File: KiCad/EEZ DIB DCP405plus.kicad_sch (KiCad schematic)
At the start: 20 parts

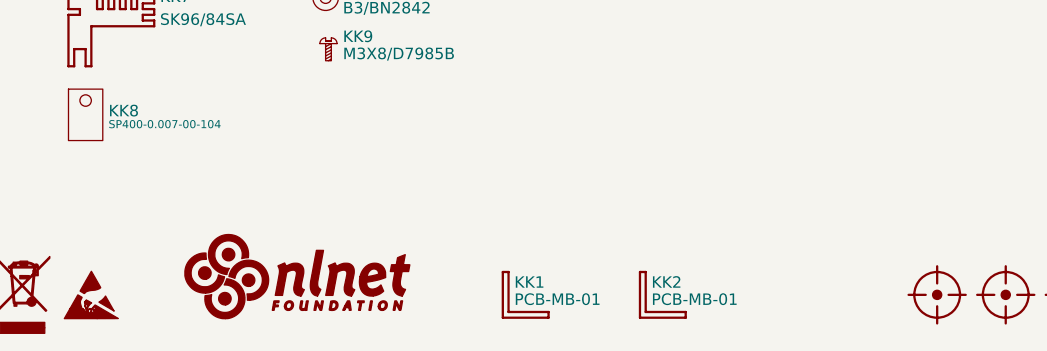
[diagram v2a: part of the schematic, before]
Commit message: OSHWA logo added, KiCad 10 migration
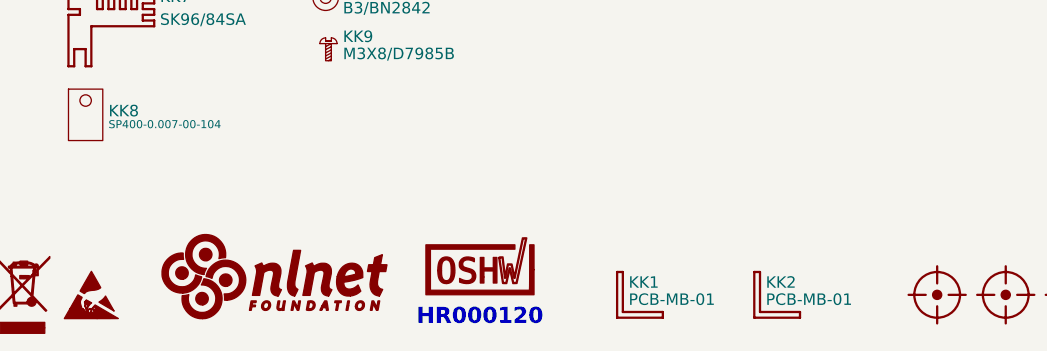
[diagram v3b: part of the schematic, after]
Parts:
- added LOGO7: OSHWA logo, PCM_EEZ_unsorted:OSHWA logo 6.6mm, symbol PCM_EEZ_symbols:OSHWA logo
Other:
- note added: "HR000120"
- moved on the sheet: KK1, KK2

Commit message: BOM and Gerbers update
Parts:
- KK1, KK2: LCSC (none) -> C959626
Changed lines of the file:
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@@
+			)
+		)
+		(property "LCSC" "C959626"
+			(at 111.76 193.04 0)
+			(hide yes)
+			(show_name no)
+			(do_not_autoplace no)
+			(effects
+				(font
+					(size 0.889 0.889)
+				)
 			)
 		)
@@
 				)
 			)
+		)
+		(property "LCSC" "C959626"
+			(at 127 193.04 0)
+			(hide yes)
+			(show_name no)
+			(do_not_autoplace no)
+			(effects
+				(font
+					(size 0.889 0.889)
+				)
+			)

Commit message: #8, schematics annotated
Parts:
- renumbered KK3 to KK1, KK2 to KK10, KK4 to KK2, KK5 to KK3, KK6 to KK4, KK7 to KK5, KK8 to KK6, KK9 to KK7, KK10 to KK8, KK1 to KK9
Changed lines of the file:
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@@
 	(title_block
 		(title "${project_name}")
-		(date "2026-05-10")
+		(date "2026-06-26")
 		(rev "${project_version}")
 		(company "${project_creator}")
@@
 		(in_pos_files yes)
 		(dnp no)
-		(property "Reference" "KK1"
+		(property "Reference" "KK9"
 			(at 113.03 189.865 0)
 			(show_name no)
@@
 			(project "EEZ DIB DCP405plus"
 				(path "/65943c0e-8943-4d2a-93dc-fb4938f73312"
-					(reference "KK1")
+					(reference "KK9")
 					(unit 1)
 				)
@@
 		(dnp no)
 		(fields_autoplaced yes)
-		(property "Reference" "KK3"
+		(property "Reference" "KK1"
 			(at 22.86 157.48 0)
 			(show_name no)
@@
 			(project "EEZ DIB DCP405plus"
 				(path "/65943c0e-8943-4d2a-93dc-fb4938f73312"
-					(reference "KK3")
+					(reference "KK1")
 					(unit 1)
 				)
@@
 		(dnp no)
 		(fields_autoplaced yes)
-		(property "Reference" "KK6"
+		(property "Reference" "KK4"
 			(at 22.86 172.72 0)
 			(show_name no)
@@
 			(project "EEZ DIB DCP405plus"
 				(path "/65943c0e-8943-4d2a-93dc-fb4938f73312"
-					(reference "KK6")
+					(reference "KK4")
 					(unit 1)
 				)
@@
 		(in_pos_files yes)
 		(dnp no)
-		(property "Reference" "KK2"
+		(property "Reference" "KK10"
 			(at 128.27 189.865 0)
 			(show_name no)
@@
 			(project "EEZ DIB DCP405plus"
 				(path "/65943c0e-8943-4d2a-93dc-fb4938f73312"
-					(reference "KK2")
+					(reference "KK10")
 					(unit 1)
 				)
@@
 		(dnp no)
 		(fields_autoplaced yes)
-		(property "Reference" "KK9"
+		(property "Reference" "KK7"
 			(at 81.28 162.56 0)
 			(show_name no)
@@
 			(project "EEZ DIB DCP405plus"
 				(path "/65943c0e-8943-4d2a-93dc-fb4938f73312"
-					(reference "KK9")
+					(reference "KK7")
 					(unit 1)
 				)
@@
 		(in_pos_files yes)
 		(dnp no)
-		(property "Reference" "KK7"
+		(property "Reference" "KK5"
 			(at 60.96 158.115 0)
 			(show_name no)
@@
 			(project "EEZ DIB DCP405plus"
 				(path "/65943c0e-8943-4d2a-93dc-fb4938f73312"
-					(reference "KK7")
+					(reference "KK5")
 					(unit 1)
 				)
@@
 		(dnp no)
 		(fields_autoplaced yes)
-		(property "Reference" "KK8"
+		(property "Reference" "KK6"
 			(at 55.245 170.815 0)
 			(show_name no)
@@
 			(project "EEZ DIB DCP405plus"
 				(path "/65943c0e-8943-4d2a-93dc-fb4938f73312"
-					(reference "KK8")
+					(reference "KK6")
 					(unit 1)
 				)
@@
 		(dnp no)
 		(fields_autoplaced yes)
-		(property "Reference" "KK5"
+		(property "Reference" "KK3"
 			(at 22.86 167.64 0)
 			(show_name no)
@@
 			(project "EEZ DIB DCP405plus"
 				(path "/65943c0e-8943-4d2a-93dc-fb4938f73312"
-					(reference "KK5")
+					(reference "KK3")
 					(unit 1)
 				)
@@
 		(in_pos_files yes)
 		(dnp no)
-		(property "Reference" "KK10"
+		(property "Reference" "KK8"
 			(at 81.28 157.48 0)
 			(show_name no)
@@
 			(project "EEZ DIB DCP405plus"
 				(path "/65943c0e-8943-4d2a-93dc-fb4938f73312"
-					(reference "KK10")
+					(reference "KK8")
 					(unit 1)
 				)
@@
 		(dnp no)
 		(fields_autoplaced yes)
-		(property "Reference" "KK4"
+		(property "Reference" "KK2"
 			(at 22.86 162.56 0)
 			(show_name no)
@@
 			(project "EEZ DIB DCP405plus"
 				(path "/65943c0e-8943-4d2a-93dc-fb4938f73312"
-					(reference "KK4")
-					(unit 1)
-				)
+					(reference "KK2")
+					(unit 1)
+				)
